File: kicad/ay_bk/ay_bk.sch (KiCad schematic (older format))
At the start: 22 parts, among them J1 AudioJack3, J2 Conn_01x19_Male, SW1 SW_Push, U1 74HCT02, U2 74HCT193, U3 YM2149, Y1 12000 KHZ

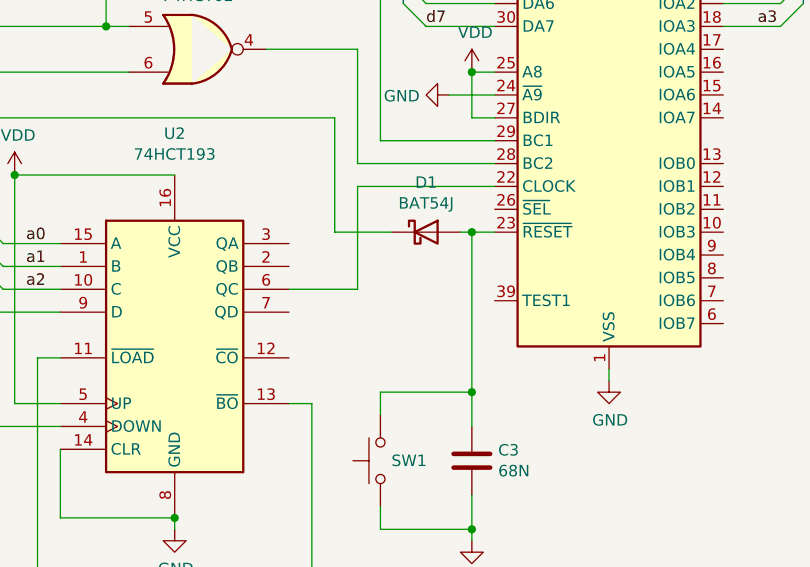
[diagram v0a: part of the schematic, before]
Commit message: improve reset circuit
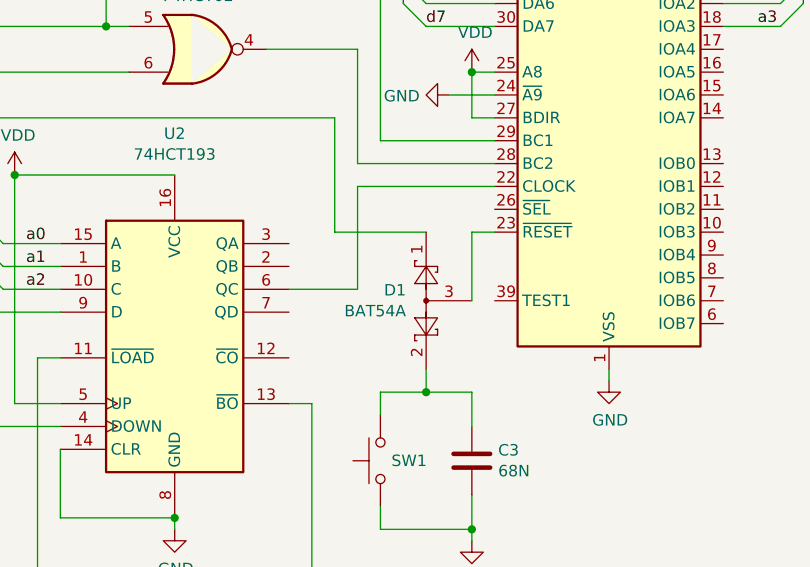
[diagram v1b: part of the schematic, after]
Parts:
- removed D1: BAT54J, Diode_SMD:D_SOD-323_HandSoldering, symbol Diode:BAT54J
- added D1: BAT54A, Package_TO_SOT_SMD:SOT-23, symbol Diode:BAT54A
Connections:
- net RST: now also D1.1
- net at C3.1, SW1.2: now also D1.2; no longer U3.23 (~RESET)
- new net: D1.3, U3.23 (~RESET)
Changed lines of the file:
@@
 Sheet 1 1
 Title "Universal AY for BK0010/11M"
-Date ""
-Rev "0.1"
+Date "2021-04-09"
+Rev "0.2"
 Comp "stanislav.maslovski@gmail.com"
 Comment1 "Stanislav Maslovski"
@@
 Text Label 8000 1300 0    50   ~ 0
 L
-$Comp
-L Diode:BAT54J D1
-U 1 1 5F97ADA7
-P 4500 3500
-F 0 "D1" H 4500 3717 50  0000 C CNN
-F 1 "BAT54J" H 4500 3626 50  0000 C CNN
-F 2 "Diode_SMD:D_SOD-323_HandSoldering" H 4500 3500 50  0001 C CNN
-F 3 "~" H 4500 3500 50  0001 C CNN
-	1    4500 3500
-	1    0    0    -1
-$EndComp
-Wire Wire Line
-	4650 3500 4700 3500
 Entry Wire Line
 	1400 3200 1500 3300
@@
 Wire Wire Line
 	4100 3000 4100 3500
-Wire Wire Line
-	4100 3500 4350 3500
 $Comp
 L Device:C C3
@@
 	1    0    0    -1
 $EndComp
-Connection ~ 4700 3500
-Wire Wire Line
-	4700 3500 4800 3500
 $Comp
 L Switch:SW_Push SW1
@@
 $EndComp
 Wire Wire Line
-	4700 3500 4700 4200
-Wire Wire Line
 	4300 4300 4300 4200
 Wire Wire Line
-	4300 4200 4700 4200
-Connection ~ 4700 4200
+	4300 4200 4500 4200
 Wire Wire Line
 	4700 4200 4700 4350
@@
 Wire Wire Line
 	8200 2100 8400 2100
+Wire Wire Line
+	8400 2150 8400 2400
+$Comp
+L Diode:BAT54A D1
+U 1 1 6070E392
+P 4500 3800
+F 0 "D1" V 4454 3888 50  0000 L CNN
+F 1 "BAT54A" V 4545 3888 50  0000 L CNN
+F 2 "Package_TO_SOT_SMD:SOT-23" H 4575 3925 50  0001 L CNN
+F 3 "http://www.diodes.com/_files/datasheets/ds11005.pdf" H 4380 3800 50  0001 C CNN
+	1    4500 3800
+	0    -1   1    0
+$EndComp
+Wire Wire Line
+	4100 3500 4500 3500
+Wire Wire Line
+	4500 4100 4500 4200
+Connection ~ 4500 4200
+Wire Wire Line
+	4500 4200 4700 4200
+Wire Wire Line
+	4700 3800 4700 3500
+Wire Wire Line
+	4700 3500 4800 3500
 Wire Bus Line
 	4400 1100 8100 1100
@@
 Wire Bus Line
 	1400 1100 1400 3200
-Wire Wire Line
-	8400 2150 8400 2400
 $EndSCHEMATC
